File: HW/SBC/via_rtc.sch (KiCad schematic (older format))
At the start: 7 parts, among them J2 CONN_02X07, J3 CONN_02X07, U6 WD65C22, U7 DS1511Y+

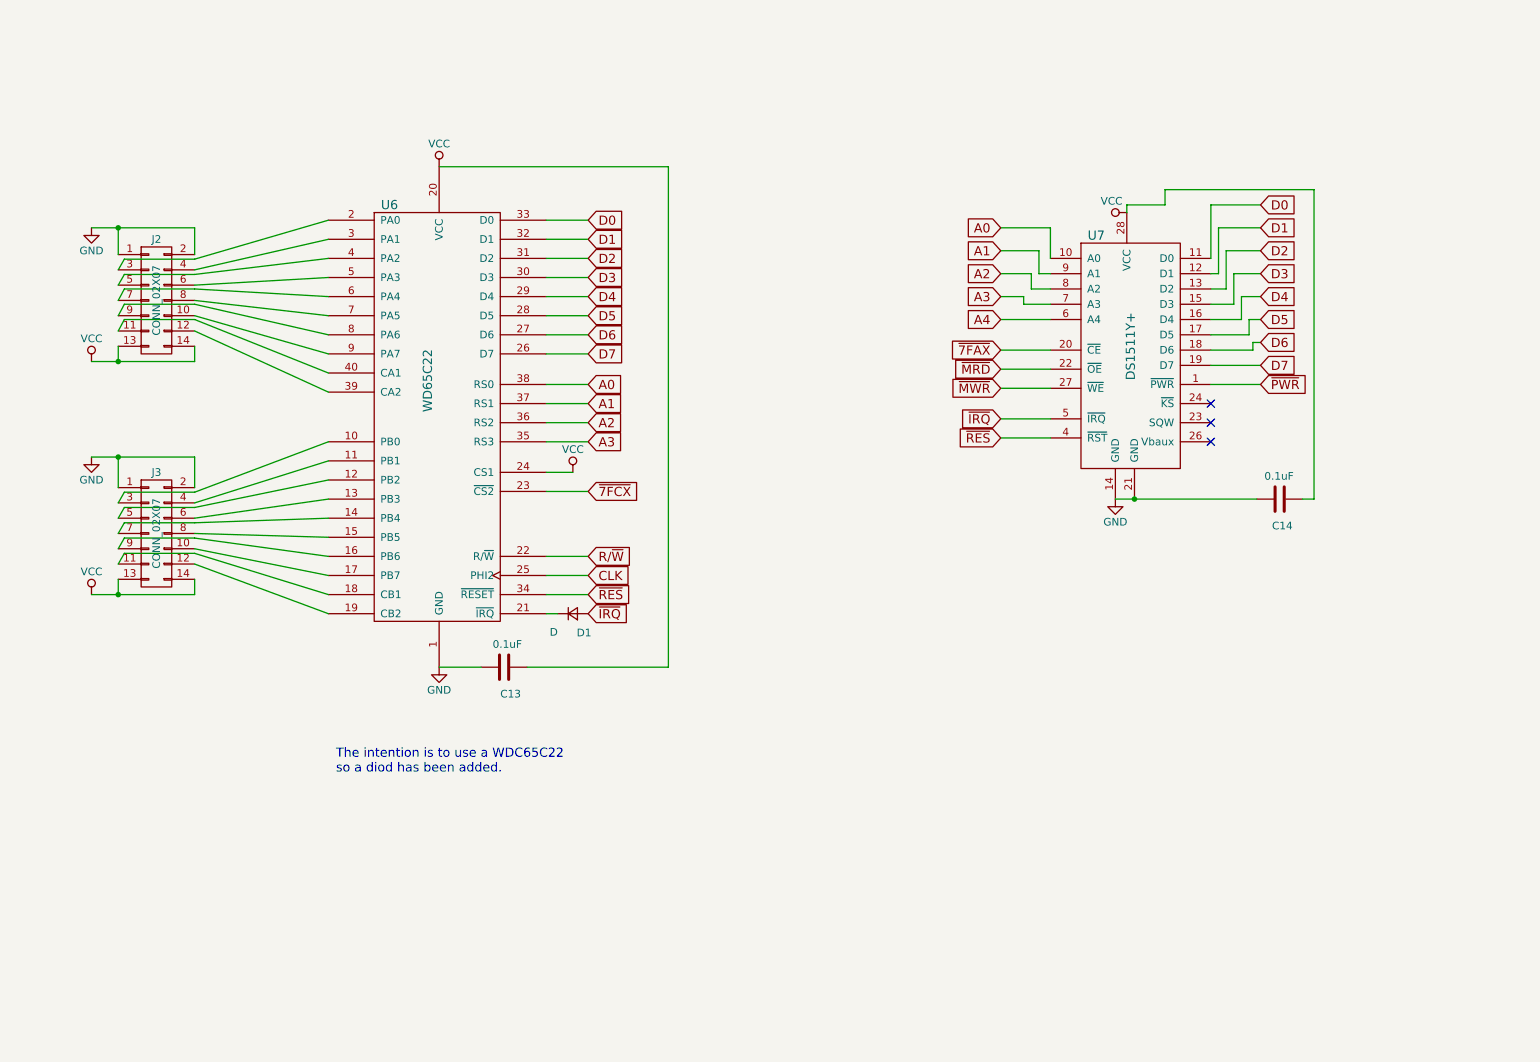
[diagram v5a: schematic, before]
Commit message: New schema. Adding a VIA and sound chip.
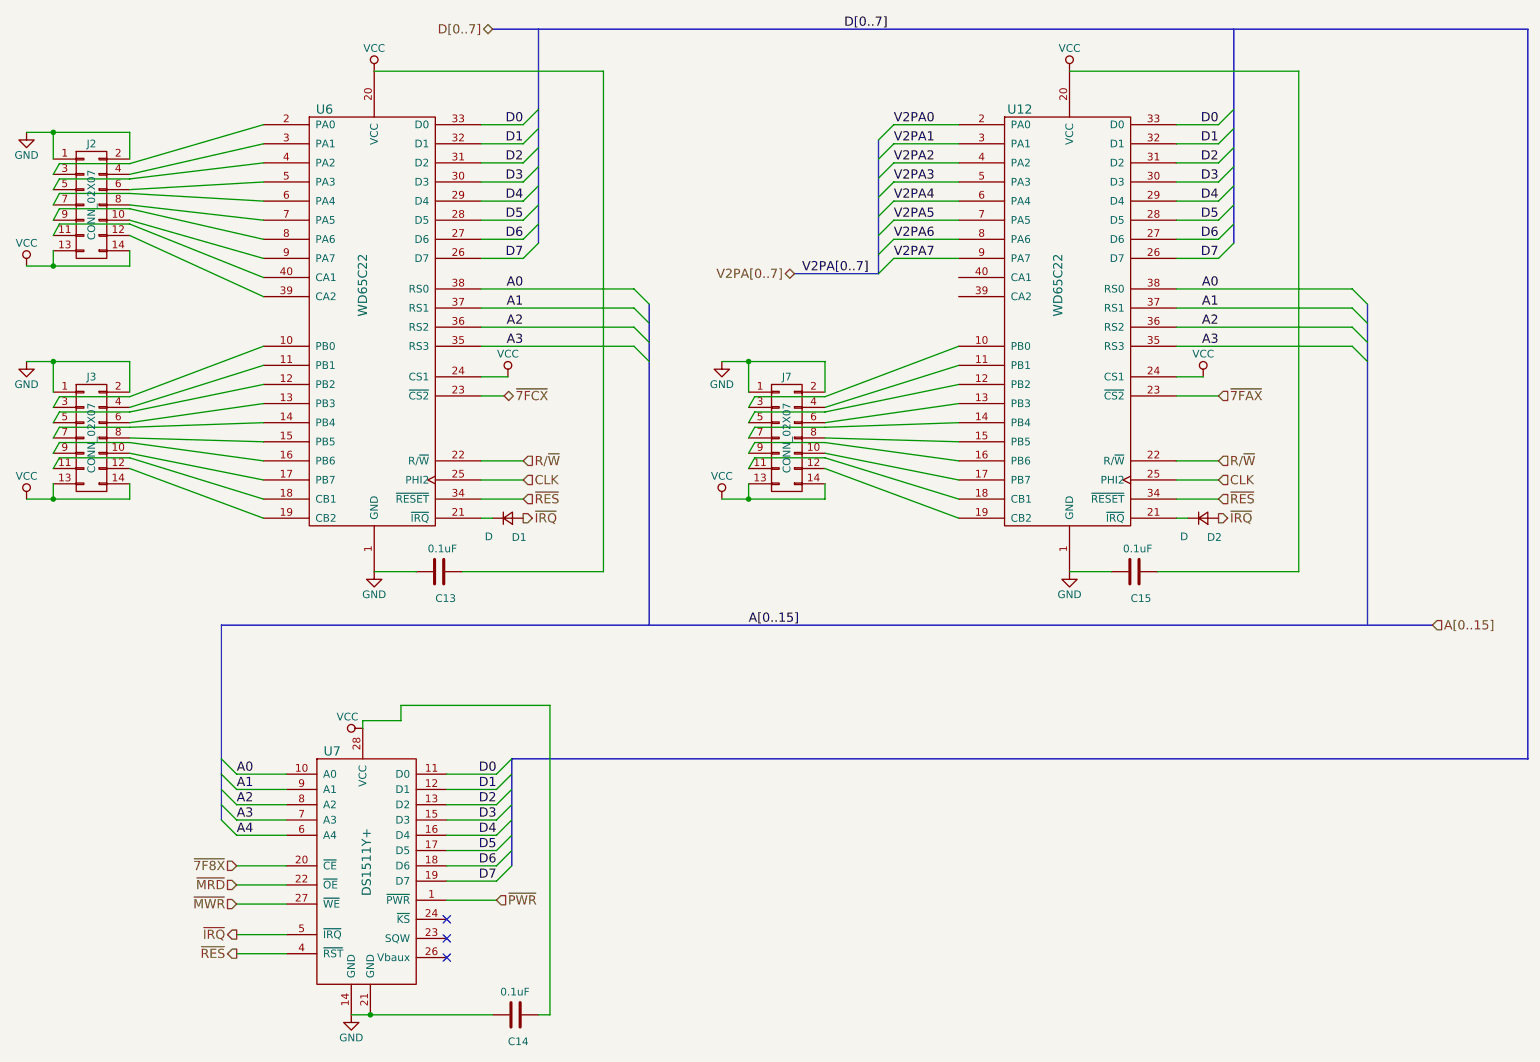
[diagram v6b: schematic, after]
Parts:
- added C15: 0.1uF, Capacitors_ThroughHole:C_Disc_D3.8mm_W2.6mm_P2.50mm, symbol C
- added D2: D, Diodes_ThroughHole:D_DO-35_SOD27_P7.62mm_Horizontal, symbol D_Small
- added J7: CONN_02X07, Connect:IDC_Header_Straight_14pins, symbol CONN_02X07
- added U12: WD65C22, Housings_DIP:DIP-40_W15.24mm, symbol WD65C22
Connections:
- net A0: now also U12.38 (RS0)
- net A1: now also U12.37 (RS1)
- net A2: now also U12.36 (RS2)
- net A3: now also U12.35 (RS3)
- net CLK: now also U12.25 (PHI2)
- net D0: now also U12.33 (D0)
- net D1: now also U12.32 (D1)
- net D2: now also U12.31 (D2)
- net D3: now also U12.30 (D3)
- net D4: now also U12.29 (D4)
- net D5: now also U12.28 (D5)
- net D6: now also U12.27 (D6)
- net D7: now also U12.26 (D7)
- net GND: now also C15.2, J7.1 (P1), J7.2 (P2), U12.1 (GND)
- net R/~W: now also U12.22 (R/~W)
- net VCC: now also C15.1, J7.13 (P13), J7.14 (P14), U12.20 (VCC), U12.24 (CS1)
- net ~7FAX: now also U12.23 (~CS2); no longer U7.20 (~CE)
- net ~IRQ: now also D2.2 (A)
- net ~RES: now also U12.34 (~RESET)
- new net: J7.3 (P3), U12.10 (PB0)
- new net: J7.4 (P4), U12.11 (PB1)
- new net: J7.5 (P5), U12.12 (PB2)
- new net: J7.6 (P6), U12.13 (PB3)
- new net: J7.7 (P7), U12.14 (PB4)
- new net: J7.8 (P8), U12.15 (PB5)
- new net: J7.9 (P9), U12.16 (PB6)
- new net: J7.10 (P10), U12.17 (PB7)
- new net: J7.11 (P11), U12.18 (CB1)
- new net: J7.12 (P12), U12.19 (CB2)
- new net: D2.1 (K), U12.21 (~IRQ)
- new net V2PA0: U12.2 (PA0)
- new net V2PA1: U12.3 (PA1)
- new net V2PA2: U12.4 (PA2)
- new net V2PA3: U12.5 (PA3)
- new net V2PA4: U12.6 (PA4)
- new net V2PA5: U12.7 (PA5)
- new net V2PA6: U12.8 (PA6)
- new net V2PA7: U12.9 (PA7)
- new net ~7F8X: U7.20 (~CE)
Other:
- note removed: "The intention is to use a WDC65C22\nso a diod has been added."
- moved on the sheet: C13, C14, D1, J2, J3, U6, U7

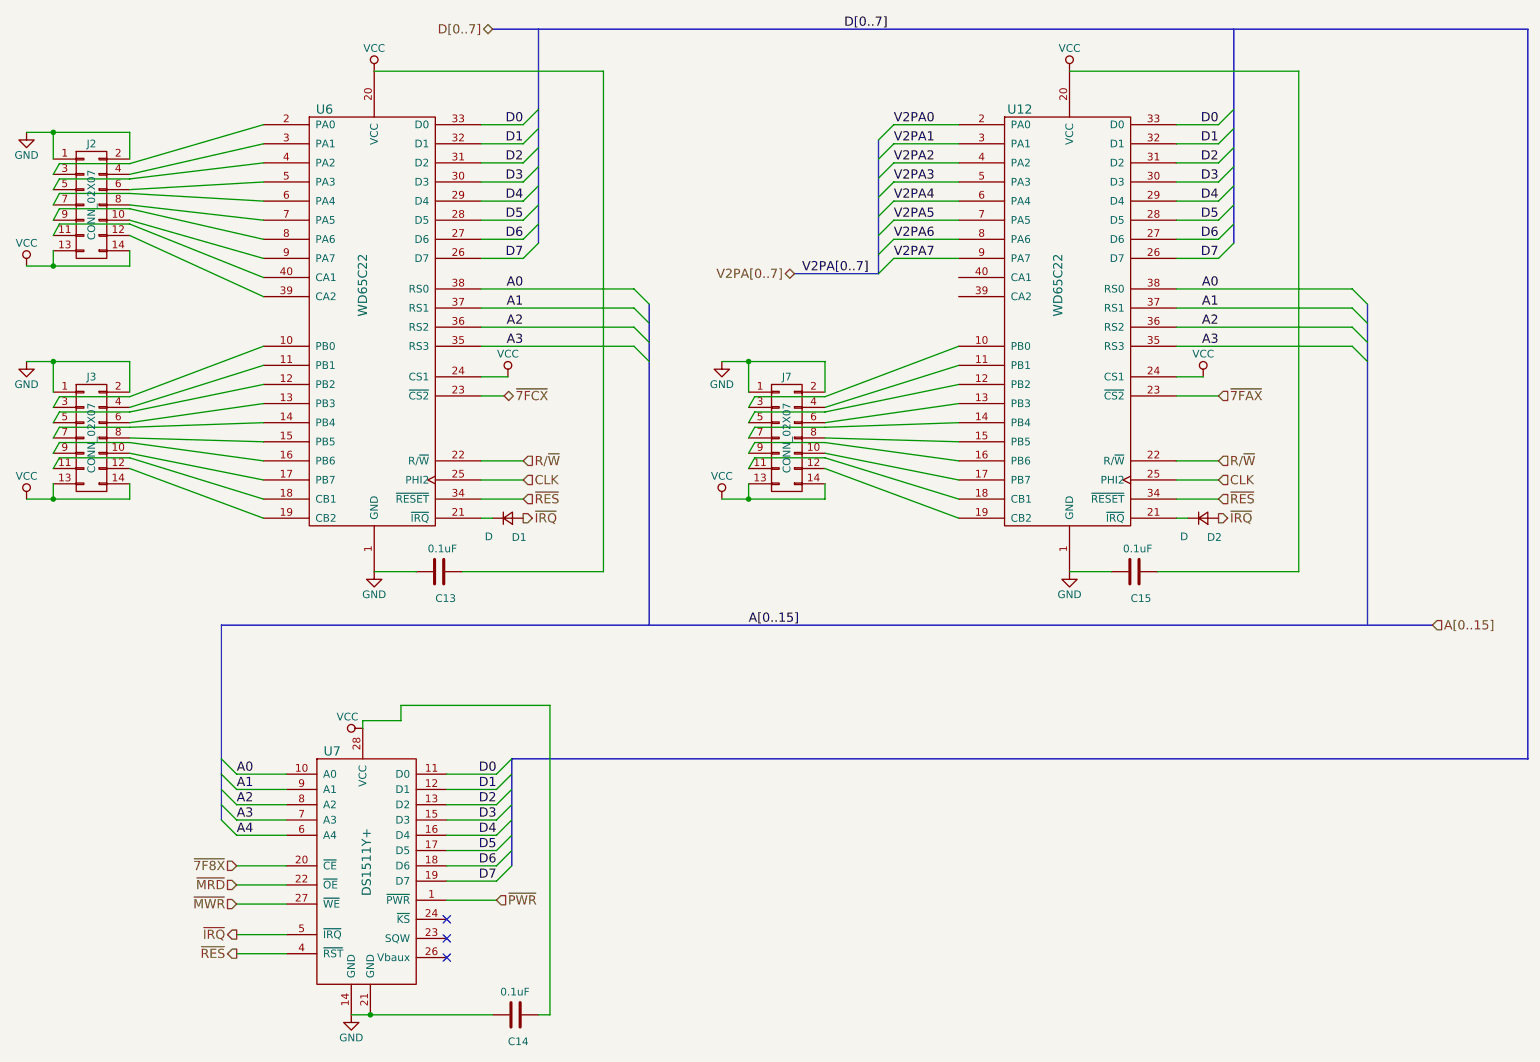
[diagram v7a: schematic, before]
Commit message: Added IDE interface to PLUTO board.
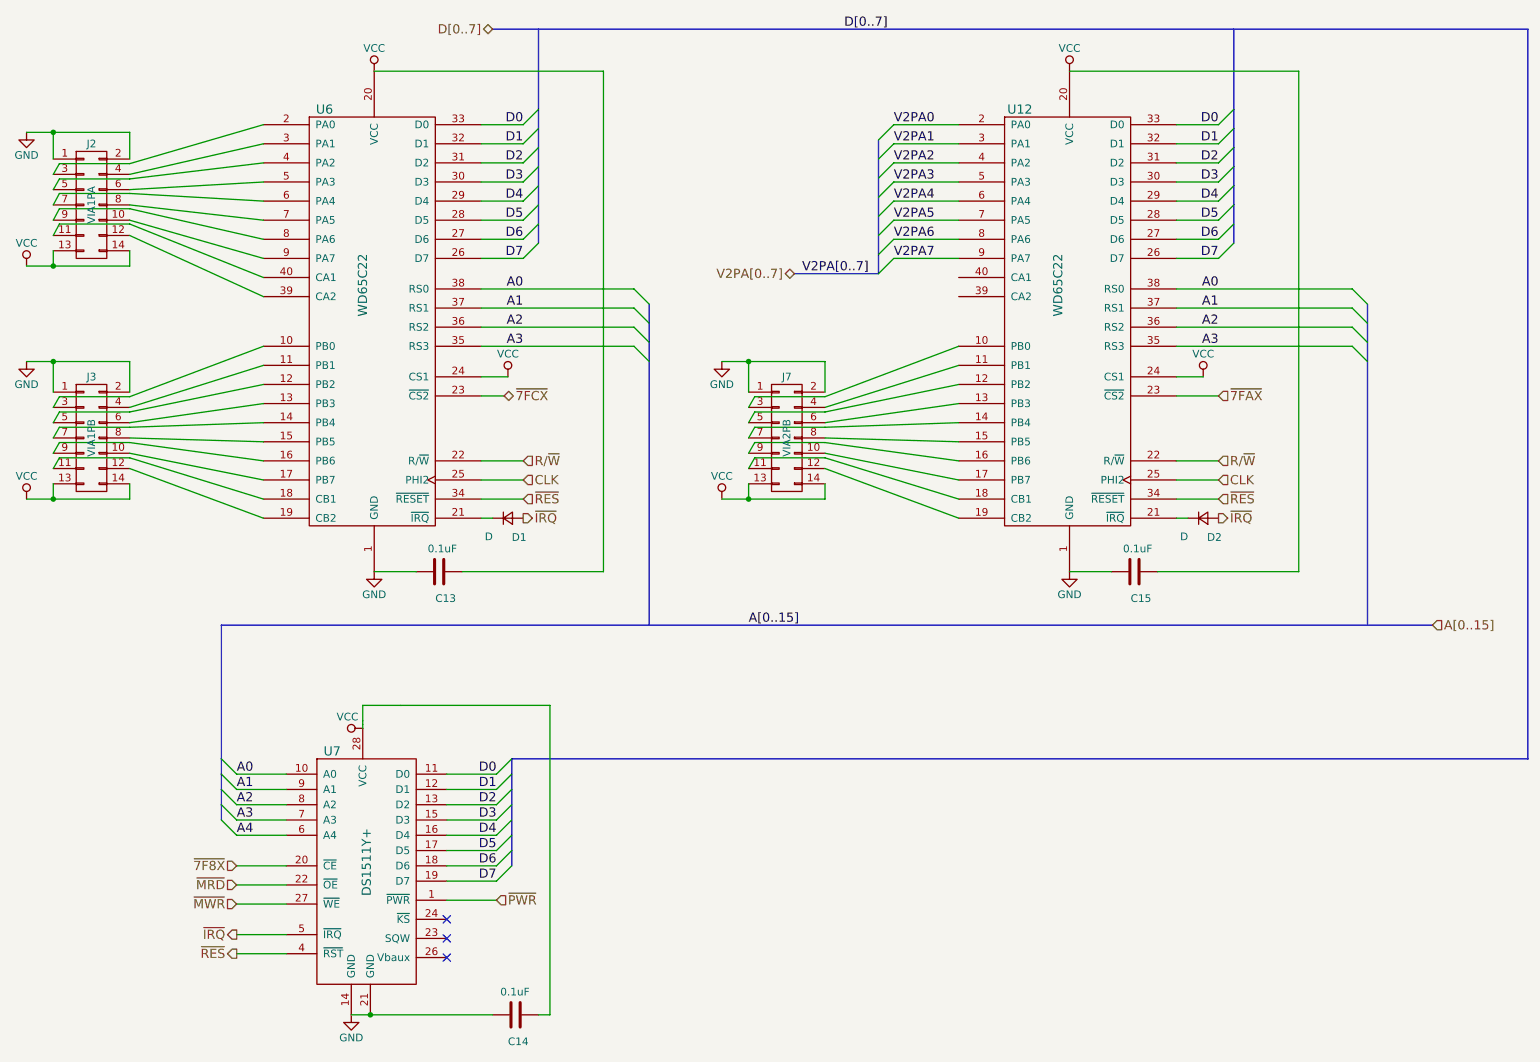
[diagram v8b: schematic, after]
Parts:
- J2: value CONN_02X07 -> VIA1PA
- J3: value CONN_02X07 -> VIA1PB
- J7: value CONN_02X07 -> VIA2PB
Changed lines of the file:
@@
 LIBS:pluto
 LIBS:pluto-cache
+LIBS:IDE_interface-cache
 EELAYER 25 0
 EELAYER END
@@
 P 1125 1800
 F 0 "J2" H 1125 2200 50  0000 C CNN
-F 1 "CONN_02X07" V 1125 1800 50  0000 C CNN
+F 1 "VIA1PA" V 1125 1800 50  0000 C CNN
 F 2 "Connect:IDC_Header_Straight_14pins" H 1125 600 50  0001 C CNN
 F 3 "" H 1125 600 50  0001 C CNN
@@
 P 1125 3325
 F 0 "J3" H 1125 3725 50  0000 C CNN
-F 1 "CONN_02X07" V 1125 3325 50  0000 C CNN
+F 1 "VIA1PB" V 1125 3325 50  0000 C CNN
 F 2 "Connect:IDC_Header_Straight_14pins" H 1125 2125 50  0001 C CNN
 F 3 "" H 1125 2125 50  0001 C CNN
@@
 	1375 3725 1375 3625
 Wire Wire Line
-	700  3725 1375 3725
+	700  3725 875  3725
+Wire Wire Line
+	875  3725 1375 3725
 Wire Wire Line
 	875  3725 875  3625
@@
 	1375 2825 1375 3025
 Wire Wire Line
-	700  2825 1375 2825
+	700  2825 875  2825
+Wire Wire Line
+	875  2825 1375 2825
 Wire Wire Line
 	875  2825 875  3025
@@
 	1375 2200 1375 2100
 Wire Wire Line
-	700  2200 1375 2200
+	700  2200 875  2200
+Wire Wire Line
+	875  2200 1375 2200
 Wire Wire Line
 	875  2200 875  2100
@@
 	1375 1325 1375 1500
 Wire Wire Line
-	700  1325 1375 1325
+	700  1325 875  1325
+Wire Wire Line
+	875  1325 1375 1325
 Wire Wire Line
 	875  1325 875  1500
@@
 	3450 5625 3775 5625
 Wire Wire Line
-	2825 7100 3750 7100
+	2825 7100 2950 7100
+Wire Wire Line
+	2950 7100 3750 7100
 Wire Wire Line
 	3450 6350 3775 6350
@@
 Connection ~ 2950 7100
 Wire Wire Line
-	2900 5225 2900 5175
+	2900 5225 2900 5200
+Wire Wire Line
+	2900 5200 2900 5175
 Wire Wire Line
 	4050 7100 4125 7100
@@
 	4125 5075 3150 5075
 Wire Wire Line
-	3150 5075 3150 5175
-Wire Wire Line
-	3150 5175 2900 5175
+	3150 5075 2900 5075
+Wire Wire Line
+	2900 5075 2900 5175
 Wire Wire Line
 	4475 925  2975 925
@@
 P 5675 3325
 F 0 "J7" H 5675 3725 50  0000 C CNN
-F 1 "CONN_02X07" V 5675 3325 50  0000 C CNN
+F 1 "VIA2PB" V 5675 3325 50  0000 C CNN
 F 2 "Connect:IDC_Header_Straight_14pins" H 5675 2125 50  0001 C CNN
 F 3 "" H 5675 2125 50  0001 C CNN
@@
 	5925 3725 5925 3625
 Wire Wire Line
-	5250 3725 5925 3725
+	5250 3725 5425 3725
+Wire Wire Line
+	5425 3725 5925 3725
 Wire Wire Line
 	5425 3725 5425 3625
@@
 	5925 2825 5925 3025
 Wire Wire Line
-	5250 2825 5925 2825
+	5250 2825 5425 2825
+Wire Wire Line
+	5425 2825 5925 2825
 Wire Wire Line
 	5425 2825 5425 3025
@@
 	6275 2250 6375 2150
 Wire Bus Line
-	6275 1375 6275 2250
+	6275 1375 6275 1500
+Wire Bus Line
+	6275 1500 6275 1625
+Wire Bus Line
+	6275 1625 6275 1750
+Wire Bus Line
+	6275 1750 6275 1875
+Wire Bus Line
+	6275 1875 6275 2000
+Wire Bus Line
+	6275 2000 6275 2125
+Wire Bus Line
+	6275 2125 6275 2250
 Wire Bus Line
 	6275 2250 5725 2250
@@
 	3950 2150 4050 2050
 Wire Bus Line
-	4050 650  4050 2050
+	4050 650  4050 1175
+Wire Bus Line
+	4050 1175 4050 1300
+Wire Bus Line
+	4050 1300 4050 1425
+Wire Bus Line
+	4050 1425 4050 1550
+Wire Bus Line
+	4050 1550 4050 1675
+Wire Bus Line
+	4050 1675 4050 1800
+Wire Bus Line
+	4050 1800 4050 1925
+Wire Bus Line
+	4050 1925 4050 2050
 Wire Bus Line
 	3750 650  10525 650
 Wire Bus Line
-	8600 650  8600 2050
+	8600 650  8600 1175
+Wire Bus Line
+	8600 1175 8600 1300
+Wire Bus Line
+	8600 1300 8600 1425
+Wire Bus Line
+	8600 1425 8600 1550
+Wire Bus Line
+	8600 1550 8600 1675
+Wire Bus Line
+	8600 1675 8600 1800
+Wire Bus Line
+	8600 1800 8600 1925
+Wire Bus Line
+	8600 1925 8600 2050
 Text Label 6050 650  0    60   ~ 0
 D[0..7]
@@
 	9375 2350 9475 2450
 Wire Bus Line
-	9475 2450 9475 4550
+	9475 2450 9475 2575
+Wire Bus Line
+	9475 2575 9475 2700
+Wire Bus Line
+	9475 2700 9475 2825
+Wire Bus Line
+	9475 2825 9475 4550
 Wire Bus Line
 	1975 4550 9900 4550
 Wire Bus Line
-	4775 2450 4775 4550
+	4775 2450 4775 2575
+Wire Bus Line
+	4775 2575 4775 2700
+Wire Bus Line
+	4775 2700 4775 2825
+Wire Bus Line
+	4775 2825 4775 4550
 Text Label 5425 4550 0    60   ~ 0
 A[0..15]
@@
 	10525 5425 3875 5425
 Wire Bus Line
-	3875 5425 3875 6125
+	3875 5425 3875 5525
+Wire Bus Line
+	3875 5525 3875 5625
+Wire Bus Line
+	3875 5625 3875 5725
+Wire Bus Line
+	3875 5725 3875 5825
+Wire Bus Line
+	3875 5825 3875 5925
+Wire Bus Line
+	3875 5925 3875 6025
+Wire Bus Line
+	3875 6025 3875 6125
 Wire Wire Line
 	2400 5525 2075 5525
@@
 	1975 5825 2075 5925
 Wire Bus Line
-	1975 4550 1975 5825
+	1975 4550 1975 5425
+Wire Bus Line
+	1975 5425 1975 5525
+Wire Bus Line
+	1975 5525 1975 5625
+Wire Bus Line
+	1975 5625 1975 5725
+Wire Bus Line
+	1975 5725 1975 5825
 Text HLabel 3775 6350 2    60   Input ~ 0
 ~PWR
